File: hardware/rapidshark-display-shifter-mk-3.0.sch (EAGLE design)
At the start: 15 parts, among them Q1 IRLML2502, Q2 IRLML2502

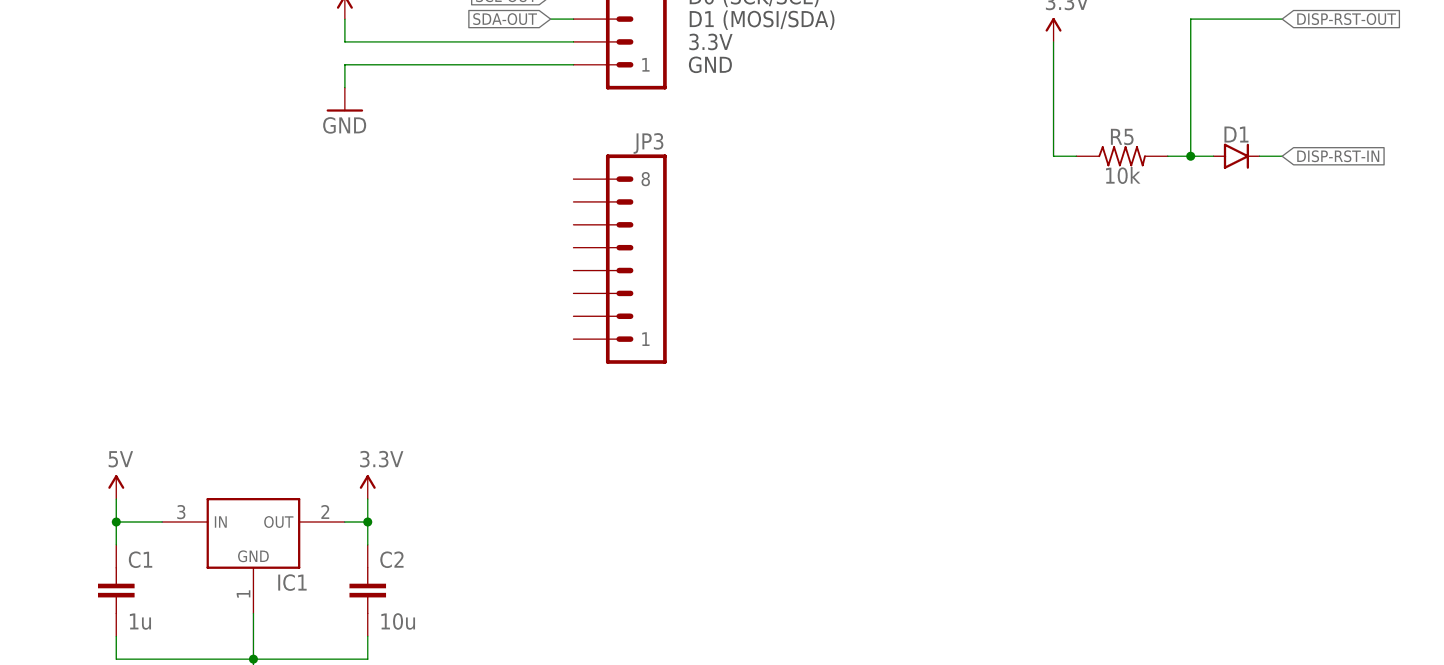
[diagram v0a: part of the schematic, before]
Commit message: layout for sf butt adapter complete
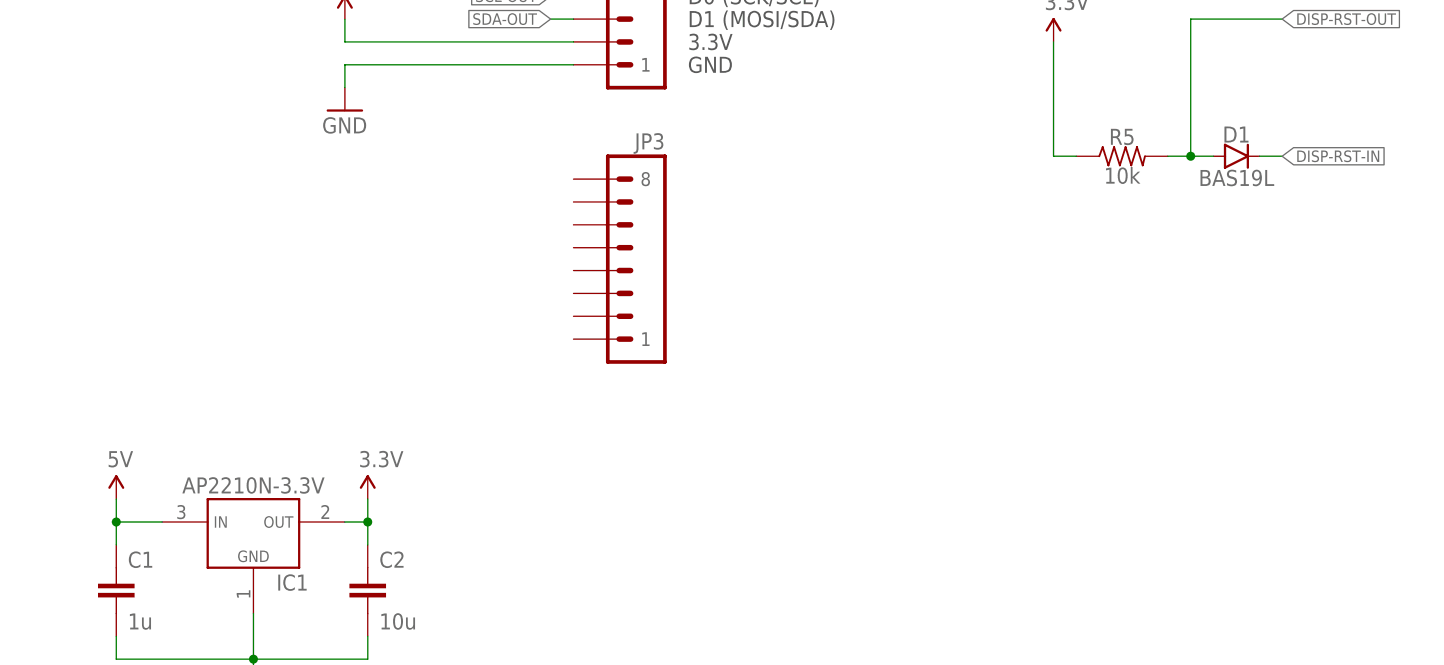
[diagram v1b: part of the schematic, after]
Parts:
- C1: device A_butts:CAPACITOR-CERAMICC0603 -> A_butts:CAPACITOR-CERAMICC0805
- D1: value (none) -> BAS19L; device A_butts:DIODESOD80 -> A_butts:DIODESOT23
- IC1: value (none) -> AP2210N-3.3V
- JP2, JP3: value (none) -> M081X08
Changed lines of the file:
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@@
 <part name="SUPPLY3" library="A_butts" deviceset="5V" device=""/>
 <part name="SUPPLY5" library="A_butts" deviceset="3.3V" device=""/>
-<part name="D1" library="A_butts" deviceset="DIODE" device="SOD80"/>
+<part name="D1" library="A_butts" deviceset="DIODE" device="SOT23" value="BAS19L"/>
 <part name="JP3" library="A_butts" deviceset="M08" device="1X08"/>
-<part name="IC1" library="A_butts" deviceset="VREG_1117" device="SOT-23"/>
-<part name="C1" library="A_butts" deviceset="CAPACITOR-CERAMIC" device="C0603" value="1u"/>
+<part name="IC1" library="A_butts" deviceset="VREG_1117" device="SOT-23" value="AP2210N-3.3V"/>
+<part name="C1" library="A_butts" deviceset="CAPACITOR-CERAMIC" device="C0805" value="1u"/>
 <part name="C2" library="A_butts" deviceset="CAPACITOR-CERAMIC" device="C0805" value="10u"/>
 <part name="SUPPLY6" library="A_butts" deviceset="3.3V" device=""/>
@@
 </sheet>
 </sheets>
-<errors>
-</errors>
 </schematic>
 </drawing>
